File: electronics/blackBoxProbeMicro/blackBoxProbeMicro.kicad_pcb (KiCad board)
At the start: 4 copper layers, 29 x 29 mm, 67 parts, among them J1 USB-C, J2 JTAG_2X05, J3 JTAG_2X05, J4 DevBoardUartOutput, Q1 BSD840N, Q2 NTJD4152P, U1 MCP1702-MB, U2 DT1446-04S, U3 STM32F103CBT, Y1 8MHz

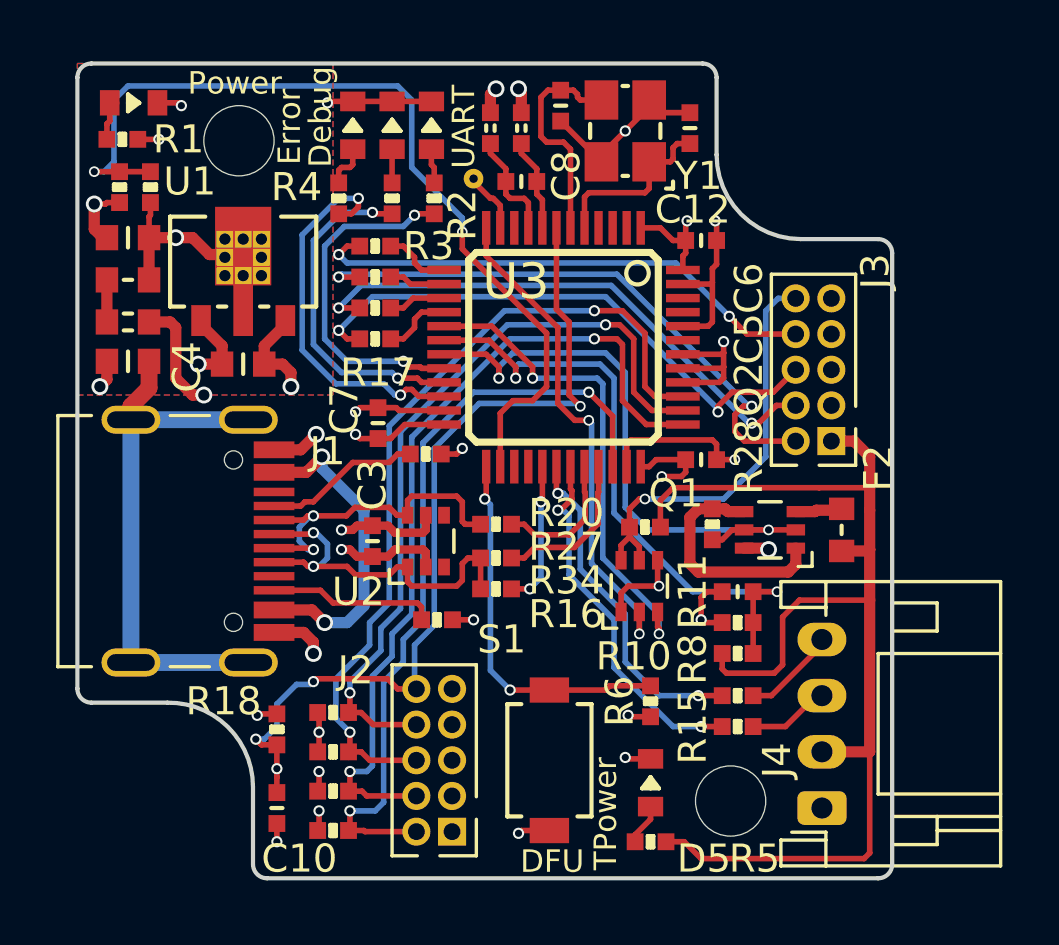
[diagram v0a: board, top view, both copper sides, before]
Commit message: removed ground plane underneath crystal oscillator section
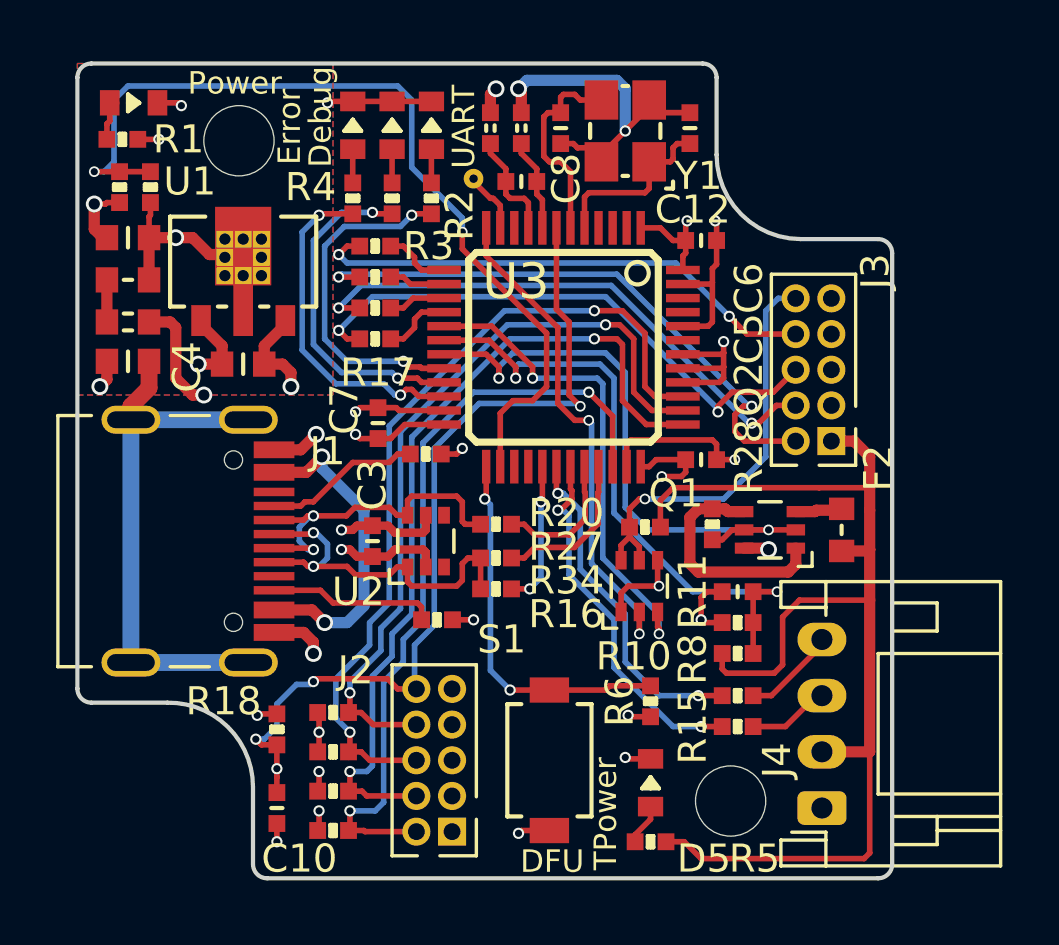
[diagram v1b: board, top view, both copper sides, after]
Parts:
- moved C13 0.80 mm to (150.2, 89.3)
- moved R4 0.50 mm to (142.8, 91.8)
- moved R2 0.10 mm to (145.6, 91.8)
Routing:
- net /VSS: track 49.2 -> 54.4 mm
- net /LED2: track 13.6 -> 12.2 mm
- net Net-(C13-Pad1): track 7.89 -> 7.36 mm

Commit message: moved JTAG out connector a bit from the edge
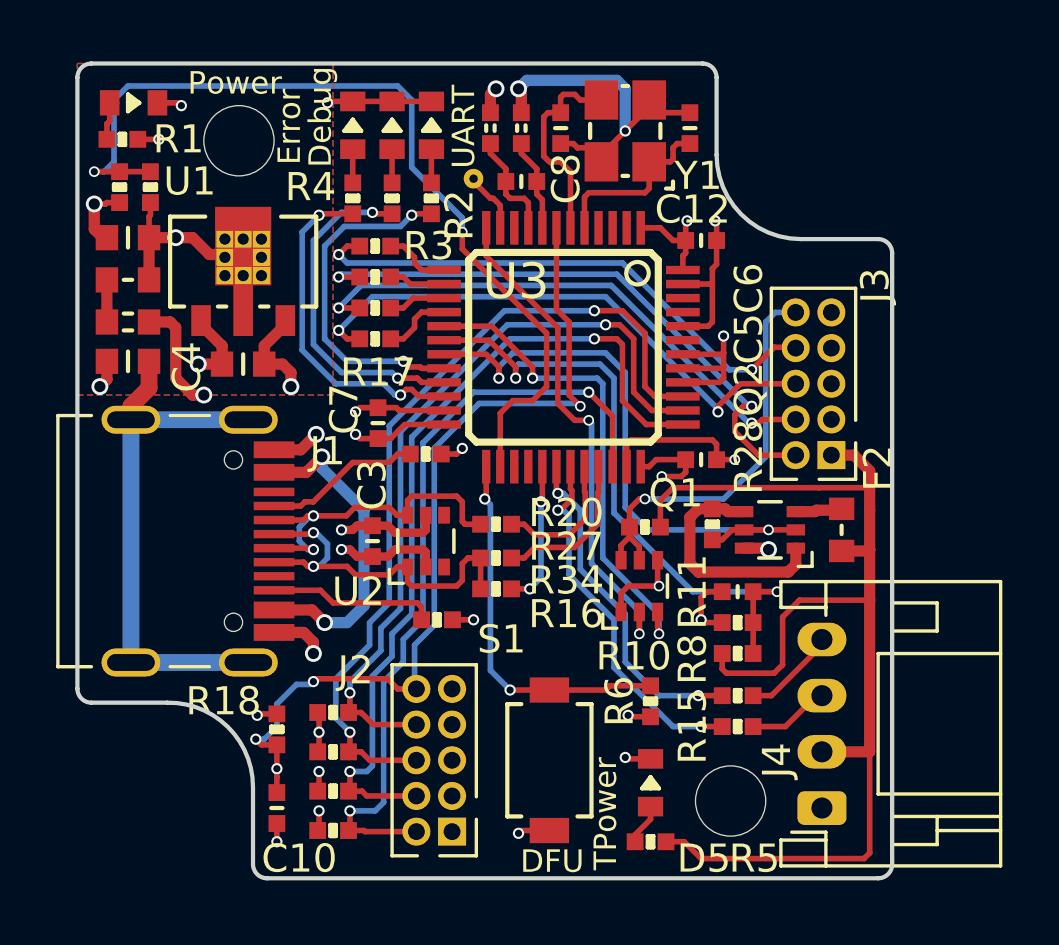
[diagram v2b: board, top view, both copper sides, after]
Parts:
- moved J3 0.50 mm to (159.2, 98.4)
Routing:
- net /PROBE_E_TDI: track 18.3 -> 19.2 mm
- net /PROBE_VDD: track 42.2 -> 41.7 mm
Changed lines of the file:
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@@
   )
   (module SquantorConnectors:Header-0127-2X05-H006 (layer F.Cu)
-    (at 159.2 97.9 90)
+    (at 159.2 98.4 90)
     (descr "Header 1.27 2by5 pins")
     (tags "Header 1.27")
@@
   (segment (start 154.65 92.65) (end 154.7 92.6) (width 0.2) (layer F.Cu) (net 4))
   (segment (start 154.65 93.3) (end 154.65 92.65) (width 0.2) (layer F.Cu) (net 4))
-  (via (at 156 96.9) (size 0.4) (drill 0.254) (layers F.Cu B.Cu) (net 4))
   (segment (start 155.95 97.35) (end 156 97.3) (width 0.2) (layer F.Cu) (net 4))
   (segment (start 154.55 97.35) (end 155.95 97.35) (width 0.2) (layer F.Cu) (net 4))
-  (segment (start 156 97.3) (end 156 96.9) (width 0.2) (layer F.Cu) (net 4))
   (segment (start 155.95 97.85) (end 156 97.8) (width 0.2) (layer F.Cu) (net 4))
   (segment (start 154.55 97.85) (end 155.95 97.85) (width 0.2) (layer F.Cu) (net 4))
@@
   (via (at 135.9 89.7) (size 0.4) (drill 0.254) (layers F.Cu B.Cu) (net 4))
   (segment (start 135.15 89.7) (end 135.9 89.7) (width 0.2) (layer F.Cu) (net 4))
+  (segment (start 156 97.3) (end 156 96.7) (width 0.2) (layer F.Cu) (net 4))
+  (via (at 156 96.7) (size 0.4) (drill 0.254) (layers F.Cu B.Cu) (net 4))
   (segment (start 149.55 92.85) (end 149.55 91.85) (width 0.2) (layer F.Cu) (net 5))
   (segment (start 149.35 91.65) (end 149.35 91.2) (width 0.2) (layer F.Cu) (net 5))
@@
   (segment (start 161.2 102.9) (end 161.2 104.3) (width 0.4) (layer F.Cu) (net 11))
   (segment (start 161.2 102.1) (end 161.2 102.9) (width 0.4) (layer F.Cu) (net 11))
-  (segment (start 161.2 101) (end 161.2 102.1) (width 0.4) (layer F.Cu) (net 11))
-  (segment (start 160.64 100.44) (end 161.2 101) (width 0.4) (layer F.Cu) (net 11))
-  (segment (start 159.835 100.44) (end 160.64 100.44) (width 0.4) (layer F.Cu) (net 11))
   (segment (start 154.2 102.1) (end 159.4 102.1) (width 0.2) (layer F.Cu) (net 11))
   (segment (start 159.4 102.1) (end 161.2 102.1) (width 0.2) (layer F.Cu) (net 11))
   (segment (start 153.75 102.55) (end 154.2 102.1) (width 0.2) (layer F.Cu) (net 11))
   (segment (start 153.75 103.2) (end 153.75 102.55) (width 0.2) (layer F.Cu) (net 11))
+  (segment (start 161.2 101.5) (end 161.2 102.1) (width 0.4) (layer F.Cu) (net 11))
+  (segment (start 160.64 100.94) (end 161.2 101.5) (width 0.4) (layer F.Cu) (net 11))
+  (segment (start 159.835 100.94) (end 160.64 100.94) (width 0.4) (layer F.Cu) (net 11))
   (segment (start 134.05 96.2) (end 134.05 94.7) (width 0.4) (layer F.Cu) (net 12))
   (segment (start 160.15 102.9) (end 160.2 102.85) (width 0.4) (layer F.Cu) (net 13))
@@
   (segment (start 147.35 104.6) (end 146.9 104.6) (width 0.2) (layer F.Cu) (net 15))
   (via (at 153.2 102.5) (size 0.381) (drill 0.254) (layers F.Cu B.Cu) (net 17))
-  (segment (start 157.94 95.36) (end 158.565 95.36) (width 0.2) (layer B.Cu) (net 17))
-  (segment (start 157.5 95.8) (end 157.94 95.36) (width 0.2) (layer B.Cu) (net 17))
-  (segment (start 157.5 101) (end 157.5 95.8) (width 0.2) (layer B.Cu) (net 17))
-  (segment (start 153.2 102.5) (end 156 102.5) (width 0.2) (layer B.Cu) (net 17))
   (segment (start 152.65 102.85) (end 152.65 103.5) (width 0.2) (layer F.Cu) (net 17))
   (segment (start 153 102.5) (end 152.65 102.85) (width 0.2) (layer F.Cu) (net 17))
@@
   (segment (start 153 104.2) (end 152.65 103.85) (width 0.2) (layer F.Cu) (net 17))
   (segment (start 153 104.68) (end 153 104.2) (width 0.2) (layer F.Cu) (net 17))
+  (segment (start 157.5 96.2) (end 157.84 95.86) (width 0.2) (layer B.Cu) (net 17))
+  (segment (start 157.5 101) (end 157.5 96.2) (width 0.2) (layer B.Cu) (net 17))
+  (segment (start 157.84 95.86) (end 158.565 95.86) (width 0.2) (layer B.Cu) (net 17))
   (segment (start 156 102.5) (end 157.5 101) (width 0.2) (layer B.Cu) (net 17))
+  (segment (start 153.2 102.5) (end 156 102.5) (width 0.2) (layer B.Cu) (net 17))
   (via (at 149.2 98.2) (size 0.4) (drill 0.254) (layers F.Cu B.Cu) (net 19))
   (via (at 153.7 107.3) (size 0.381) (drill 0.254) (layers F.Cu B.Cu) (net 19))
@@
   (segment (start 142.4 94.5) (end 152.2 94.5) (width 0.2) (layer B.Cu) (net 37))
   (segment (start 142.3 94.6) (end 142.4 94.5) (width 0.2) (layer B.Cu) (net 37))
-  (segment (start 156.74 100.44) (end 158.565 100.44) (width 0.2) (layer F.Cu) (net 37))
-  (segment (start 156.4 100.1) (end 156.74 100.44) (width 0.2) (layer F.Cu) (net 37))
+  (segment (start 157.24 100.94) (end 158.565 100.94) (width 0.2) (layer F.Cu) (net 37))
+  (segment (start 156.4 100.1) (end 157.24 100.94) (width 0.2) (layer F.Cu) (net 37))
   (segment (start 156.4 99.5) (end 156.4 100.1) (width 0.2) (layer F.Cu) (net 37))
   (segment (start 156.7 99.2) (end 156.4 99.5) (width 0.2) (layer F.Cu) (net 37))
   (segment (start 157 99.2) (end 156.7 99.2) (width 0.2) (layer F.Cu) (net 37))
-  (segment (start 157.765 98.7) (end 158.565 97.9) (width 0.2) (layer F.Cu) (net 38))
-  (segment (start 155.8 99.4) (end 155.8 99.2) (width 0.2) (layer F.Cu) (net 38))
-  (segment (start 155.8 99.2) (end 156.3 98.7) (width 0.2) (layer F.Cu) (net 38))
-  (segment (start 156.3 98.7) (end 157.765 98.7) (width 0.2) (layer F.Cu) (net 38))
   (via (at 155.8 99.4) (size 0.4) (drill 0.254) (layers F.Cu B.Cu) (net 38))
   (segment (start 151.8 95.3) (end 155.8 99.3) (width 0.2) (layer B.Cu) (net 38))
@@
   (segment (start 142.3 96.5) (end 142.6 96.8) (width 0.2) (layer F.Cu) (net 38))
   (via (at 142.3 96.5) (size 0.4) (drill 0.254) (layers F.Cu B.Cu) (net 38))
-  (segment (start 157.25 99.8) (end 157.88 99.17) (width 0.2) (layer F.Cu) (net 39))
+  (segment (start 156.6 98.4) (end 158.565 98.4) (width 0.2) (layer F.Cu) (net 38))
+  (segment (start 155.8 99.2) (end 156.6 98.4) (width 0.2) (layer F.Cu) (net 38))
+  (segment (start 155.8 99.4) (end 155.8 99.2) (width 0.2) (layer F.Cu) (net 38))
   (segment (start 152 94.9) (end 143.5 94.9) (width 0.2) (layer B.Cu) (net 39))
   (segment (start 156.9 99.8) (end 152 94.9) (width 0.2) (layer B.Cu) (net 39))
-  (segment (start 157.88 99.17) (end 158.565 99.17) (width 0.2) (layer F.Cu) (net 39))
   (segment (start 157 99.8) (end 156.9 99.8) (width 0.2) (layer B.Cu) (net 39))
-  (segment (start 157 99.8) (end 157.25 99.8) (width 0.2) (layer F.Cu) (net 39))
   (via (at 157 99.8) (size 0.4) (drill 0.254) (layers F.Cu B.Cu) (net 39))
   (via (at 142.3 95.7) (size 0.4) (drill 0.254) (layers F.Cu B.Cu) (net 39))
@@
   (segment (start 143.5 94.9) (end 143.1 94.9) (width 0.2) (layer B.Cu) (net 39))
   (segment (start 142.3 95.7) (end 143.05 95.7) (width 0.2) (layer F.Cu) (net 39))
-  (segment (start 158.565 96.63) (end 157.63 96.63) (width 0.2) (layer F.Cu) (net 40))
-  (via (at 156.2 96) (size 0.4) (drill 0.254) (layers F.Cu B.Cu) (net 40))
-  (segment (start 156.83 96.63) (end 156.2 96) (width 0.2) (layer F.Cu) (net 40))
-  (segment (start 157.63 96.63) (end 156.83 96.63) (width 0.2) (layer F.Cu) (net 40))
+  (segment (start 157.38 99.67) (end 158.565 99.67) (width 0.2) (layer F.Cu) (net 39))
+  (segment (start 157.25 99.8) (end 157.38 99.67) (width 0.2) (layer F.Cu) (net 39))
+  (segment (start 157 99.8) (end 157.25 99.8) (width 0.2) (layer F.Cu) (net 39))
   (segment (start 142.6 93.5) (end 143.05 93.5) (width 0.2) (layer F.Cu) (net 40))
   (segment (start 142.3 93.8) (end 142.6 93.5) (width 0.2) (layer F.Cu) (net 40))
-  (segment (start 142.6 94.1) (end 154.3 94.1) (width 0.2) (layer B.Cu) (net 40))
-  (segment (start 142.3 93.8) (end 142.6 94.1) (width 0.2) (layer B.Cu) (net 40))
-  (segment (start 154.3 94.1) (end 156.2 96) (width 0.2) (layer B.Cu) (net 40))
   (via (at 142.3 93.8) (size 0.4) (drill 0.254) (layers F.Cu B.Cu) (net 40))
+  (segment (start 142.6 94.1) (end 142.3 93.8) (width 0.2) (layer B.Cu) (net 40))
+  (segment (start 152.4 94.1) (end 142.6 94.1) (width 0.2) (layer B.Cu) (net 40))
+  (segment (start 157 97.9) (end 156.2 97.9) (width 0.2) (layer B.Cu) (net 40))
+  (segment (start 158.535 97.1) (end 158.565 97.13) (width 0.2) (layer F.Cu) (net 40))
+  (segment (start 157.8 97.1) (end 158.535 97.1) (width 0.2) (layer F.Cu) (net 40))
+  (segment (start 156.2 97.9) (end 152.4 94.1) (width 0.2) (layer B.Cu) (net 40))
+  (segment (start 157 97.9) (end 157.8 97.1) (width 0.2) (layer F.Cu) (net 40))
+  (via (at 157 97.9) (size 0.4) (drill 0.254) (layers F.Cu B.Cu) (net 40))
   (via (at 155.2 110.6) (size 0.4) (drill 0.254) (layers F.Cu B.Cu) (net 44))
   (segment (start 155.2 110.6) (end 155.95 110.6) (width 0.2) (layer F.Cu) (net 44))

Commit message: placement, routing, and silk optimizations
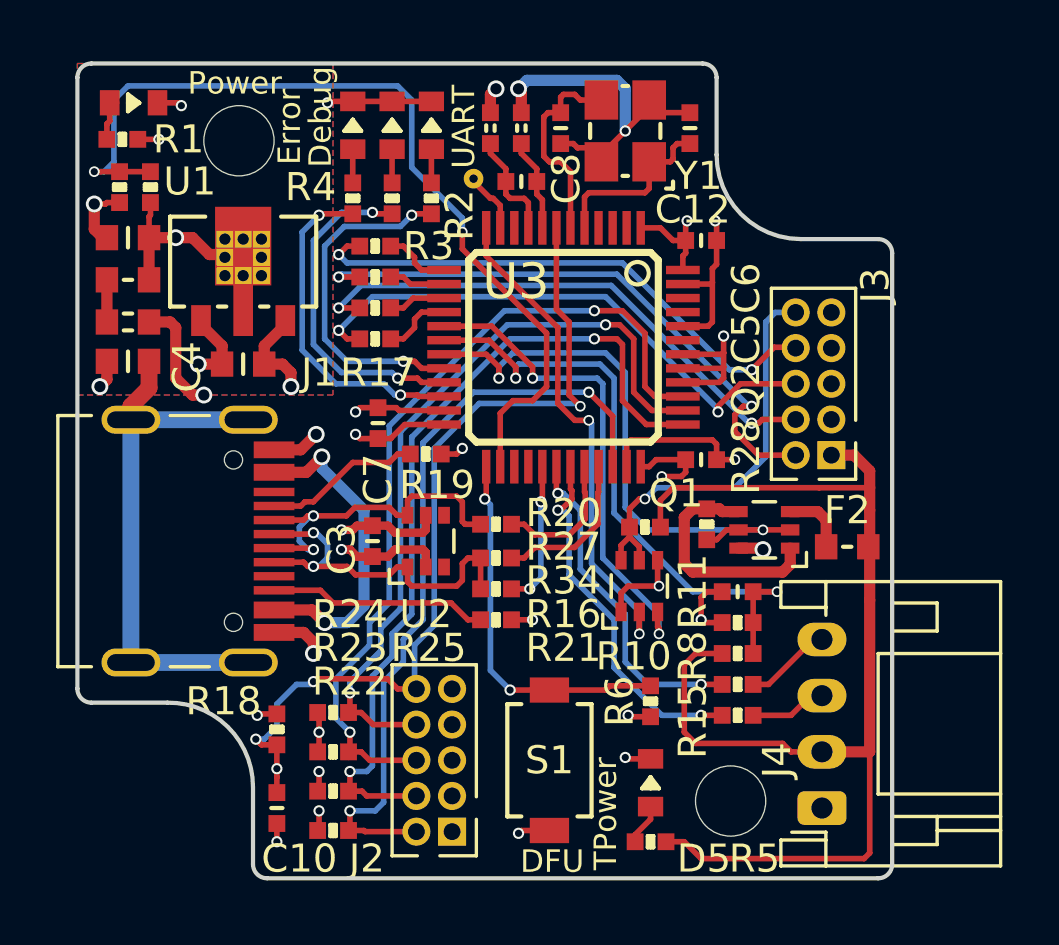
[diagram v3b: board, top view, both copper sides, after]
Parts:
- moved R21 2.10 mm to (147.9, 106.8)
- moved F2 0.63 mm to (160.4, 104.2), turned to 180 degrees
- moved R8 0.40 mm to (156.5, 109.1)
- moved R15 0.40 mm to (156.5, 110.2)
- moved Q2 0.20 mm to (157.4, 103.6)
- moved R28 0.20 mm to (155.4, 103.4)
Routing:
- net /CC2: track 5.25 -> 7.08 mm
- net Net-(F2-Pad2): track 1.67 -> 2.35 mm

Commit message: removed rescue library
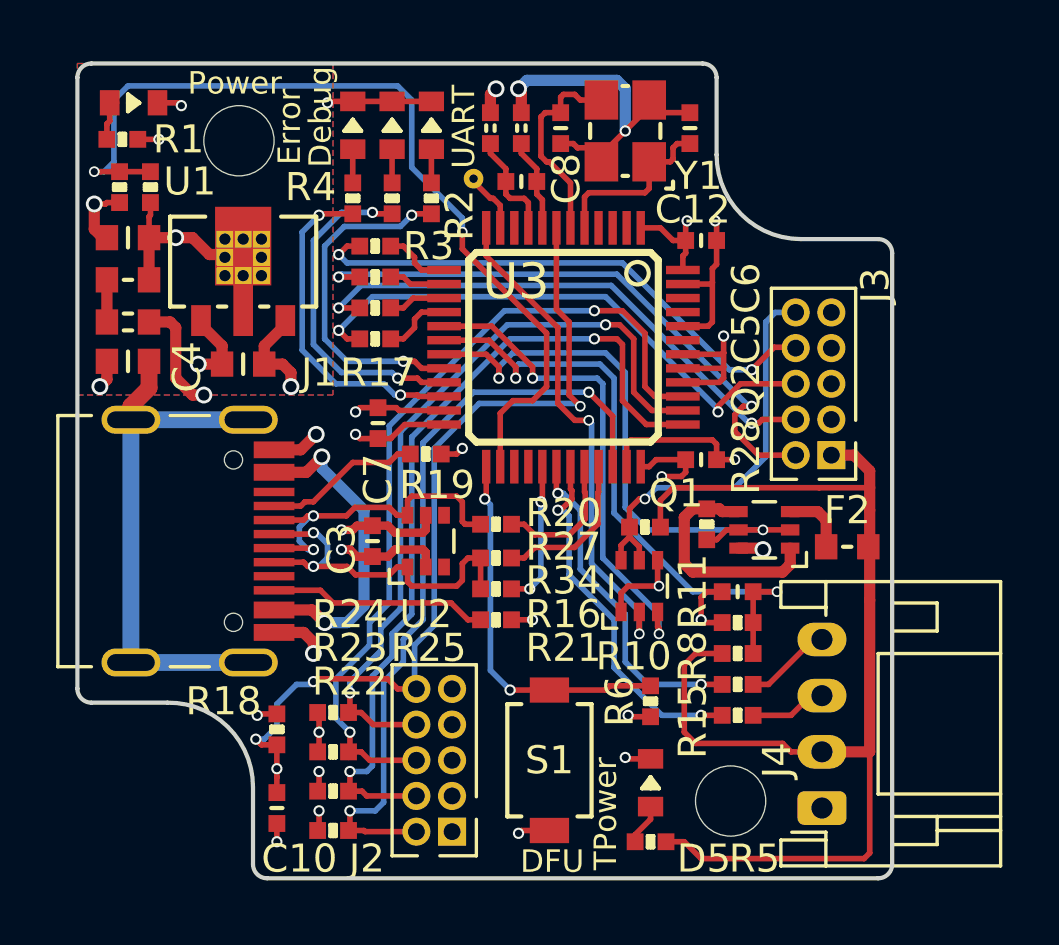
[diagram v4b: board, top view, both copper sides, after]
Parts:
- N2: value V:20210818 -> V:20230224
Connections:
- J1 pad A8: Net-(J1-PadA8) -> unconnected-(J1-PadA8)
- J1 pad B8: Net-(J1-PadB8) -> unconnected-(J1-PadB8)
- J2 pad 7: Net-(J2-Pad7) -> unconnected-(J2-Pad7)
- J3 pad 7: Net-(J3-Pad7) -> unconnected-(J3-Pad7)
- U2 pad 3: Net-(U2-Pad3) -> unconnected-(U2-Pad3)
- U2 pad 4: Net-(U2-Pad4) -> unconnected-(U2-Pad4)
- U3 pad 10: Net-(U3-Pad10) -> unconnected-(U3-Pad10)
- U3 pad 2: Net-(U3-Pad2) -> unconnected-(U3-Pad2)
- U3 pad 27: Net-(U3-Pad27) -> unconnected-(U3-Pad27)
- U3 pad 28: Net-(U3-Pad28) -> unconnected-(U3-Pad28)
- U3 pad 3: Net-(U3-Pad3) -> unconnected-(U3-Pad3)
- U3 pad 4: Net-(U3-Pad4) -> unconnected-(U3-Pad4)
- U3 pad 43: Net-(U3-Pad43) -> unconnected-(U3-Pad43)
- U3 pad 45: Net-(U3-Pad45) -> unconnected-(U3-Pad45)
- U3 pad 46: Net-(U3-Pad46) -> unconnected-(U3-Pad46)
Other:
- outline, holes or cut-outs redrawn
- net class Default removed
